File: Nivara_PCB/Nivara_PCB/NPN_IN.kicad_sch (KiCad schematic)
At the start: 5 parts, among them U6 LTV-357T

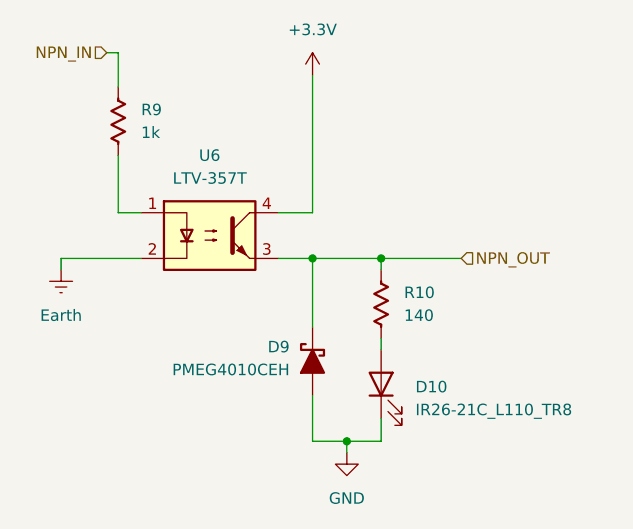
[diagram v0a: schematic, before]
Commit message: Cambios finales en la comprobación del DRC.
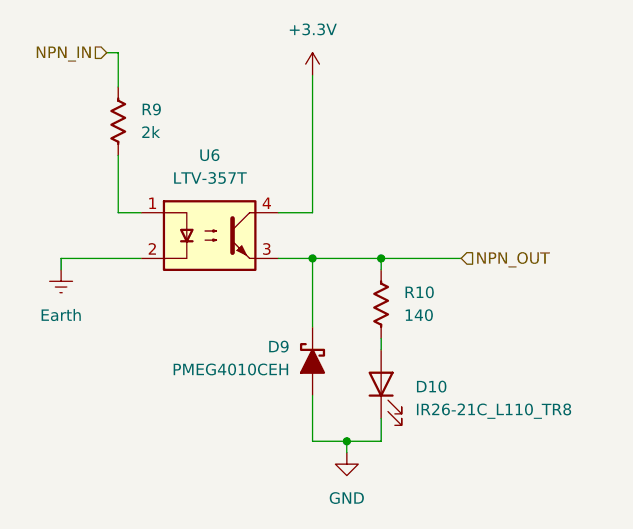
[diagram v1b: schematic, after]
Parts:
- R9: value 1k -> 2k
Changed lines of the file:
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@@
 			)
 		)
-		(property "Value" "1k"
+		(property "Value" "2k"
 			(at 107.95 68.5799 0)
 			(effects

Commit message: TERMINACIONES Y AJUSTES FINALES
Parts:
- removed D10: IR26-21C_L110_TR8, LED_SMD:LED_1206_3216Metric, symbol LED:IR26-21C_L110_TR8
- added D11: LED, LED_SMD:LED_0603_1608Metric, symbol EasyEDA:LED
- D10: renamed from D9; LCSC Part (none) -> C193342; Part # (none) -> PMEG4010CEH,115
- R13: renamed from R9; LCSC Part (none) -> C22975; Part # (none) -> 0603WAF2001T5E
- R14: renamed from R10; LCSC Part (none) -> C245910; Part # (none) -> RC0603FR-07140RL
- U8: renamed from U6; LCSC Part (none) -> C119091; Part # (none) -> LTV-357T-C
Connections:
- net GND: now also D11.1 (K)
- net at R14.2: now also D11.2 (A)
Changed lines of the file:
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@@
 		(dnp no)
 		(fields_autoplaced yes)
-		(property "Reference" "#PWR027"
+		(property "Reference" "#PWR031"
 			(at 127 66.04 0)
 			(effects
@@
 			(project "Nivara_PCB"
 				(path "/13184db0-a71d-4054-b13a-bbf46d2b100d/4e7fa7f2-8bf5-4f9c-874d-fa1b4fd76f92/0a310172-7d8e-4fb6-834e-e52959d34ba2"
-					(reference "#PWR055")
-					(unit 1)
-				)
-				(path "/13184db0-a71d-4054-b13a-bbf46d2b100d/4e7fa7f2-8bf5-4f9c-874d-fa1b4fd76f92/58467d6c-1433-4318-a1ea-3b041dc0b319"
-					(reference "#PWR027")
+					(reference "#PWR059")
+					(unit 1)
+				)
+				(path "/13184db0-a71d-4054-b13a-bbf46d2b100d/4e7fa7f2-8bf5-4f9c-874d-fa1b4fd76f92/58467d6c-1433-4318-a1ea-3b041dc0b319"
+					(reference "#PWR031")
 					(unit 1)
 				)
@@
 		(dnp no)
 		(fields_autoplaced yes)
-		(property "Reference" "#PWR028"
+		(property "Reference" "#PWR032"
 			(at 130.81 110.49 0)
 			(effects
@@
 			(project "Nivara_PCB"
 				(path "/13184db0-a71d-4054-b13a-bbf46d2b100d/4e7fa7f2-8bf5-4f9c-874d-fa1b4fd76f92/0a310172-7d8e-4fb6-834e-e52959d34ba2"
-					(reference "#PWR056")
-					(unit 1)
-				)
-				(path "/13184db0-a71d-4054-b13a-bbf46d2b100d/4e7fa7f2-8bf5-4f9c-874d-fa1b4fd76f92/58467d6c-1433-4318-a1ea-3b041dc0b319"
-					(reference "#PWR028")
+					(reference "#PWR060")
+					(unit 1)
+				)
+				(path "/13184db0-a71d-4054-b13a-bbf46d2b100d/4e7fa7f2-8bf5-4f9c-874d-fa1b4fd76f92/58467d6c-1433-4318-a1ea-3b041dc0b319"
+					(reference "#PWR032")
 					(unit 1)
 				)
@@
 		(on_board yes)
 		(dnp no)
-		(property "Reference" "D9"
+		(property "Reference" "D10"
 			(at 124.46 92.3924 90)
 			(effects
@@
 			)
 		)
-		(property "Datasheet" "https://www.tme.eu/Document/6076ddfe18935c4c311aad91dddcf920/PMEG4010CEX-DTE.pdf"
+		(property "Datasheet" "https://www.lcsc.com/datasheet/C193342.pdf"
 			(at 127 93.98 0)
 			(effects
@@
 			)
 		)
+		(property "Part #" "PMEG4010CEH,115"
+			(at 127 93.98 90)
+			(effects
+				(font
+					(size 1.27 1.27)
+				)
+				(hide yes)
+			)
+		)
+		(property "LCSC Part" "C193342"
+			(at 127 93.98 90)
+			(effects
+				(font
+					(size 1.27 1.27)
+				)
+				(hide yes)
+			)
+		)
 		(pin "1"
 		)
@@
 			(project "Nivara_PCB"
 				(path "/13184db0-a71d-4054-b13a-bbf46d2b100d/4e7fa7f2-8bf5-4f9c-874d-fa1b4fd76f92/0a310172-7d8e-4fb6-834e-e52959d34ba2"
-					(reference "D24")
-					(unit 1)
-				)
-				(path "/13184db0-a71d-4054-b13a-bbf46d2b100d/4e7fa7f2-8bf5-4f9c-874d-fa1b4fd76f92/58467d6c-1433-4318-a1ea-3b041dc0b319"
-					(reference "D9")
+					(reference "D25")
+					(unit 1)
+				)
+				(path "/13184db0-a71d-4054-b13a-bbf46d2b100d/4e7fa7f2-8bf5-4f9c-874d-fa1b4fd76f92/58467d6c-1433-4318-a1ea-3b041dc0b319"
+					(reference "D10")
 					(unit 1)
 				)
@@
 		(dnp no)
 		(fields_autoplaced yes)
-		(property "Reference" "#PWR083"
+		(property "Reference" "#PWR030"
 			(at 99.06 90.17 0)
 			(effects
@@
 			(project ""
 				(path "/13184db0-a71d-4054-b13a-bbf46d2b100d/4e7fa7f2-8bf5-4f9c-874d-fa1b4fd76f92/0a310172-7d8e-4fb6-834e-e52959d34ba2"
-					(reference "#PWR084")
-					(unit 1)
-				)
-				(path "/13184db0-a71d-4054-b13a-bbf46d2b100d/4e7fa7f2-8bf5-4f9c-874d-fa1b4fd76f92/58467d6c-1433-4318-a1ea-3b041dc0b319"
-					(reference "#PWR083")
+					(reference "#PWR058")
+					(unit 1)
+				)
+				(path "/13184db0-a71d-4054-b13a-bbf46d2b100d/4e7fa7f2-8bf5-4f9c-874d-fa1b4fd76f92/58467d6c-1433-4318-a1ea-3b041dc0b319"
+					(reference "#PWR030")
 					(unit 1)
 				)
@@
 	)
 	(symbol
-		(lib_id "LED:IR26-21C_L110_TR8")
-		(at 134.62 96.52 90)
+		(lib_id "EasyEDA:LED")
+		(at 134.62 96.52 270)
+		(mirror x)
 		(unit 1)
 		(exclude_from_sim no)
@@
 		(on_board yes)
 		(dnp no)
-		(fields_autoplaced yes)
-		(property "Reference" "D10"
-			(at 138.43 96.8374 90)
+		(property "Reference" "D11"
+			(at 144.272 96.52 90)
 			(effects
 				(font
@@
 			)
 		)
-		(property "Value" "IR26-21C_L110_TR8"
-			(at 138.43 99.3774 90)
+		(property "Value" "LED"
+			(at 144.272 99.06 90)
 			(effects
 				(font
@@
 			)
 		)
-		(property "Footprint" "LED_SMD:LED_1206_3216Metric"
-			(at 129.54 96.52 0)
-			(effects
-				(font
-					(size 1.27 1.27)
-				)
-				(hide yes)
-			)
-		)
-		(property "Datasheet" "http://www.everlight.com/file/ProductFile/IR26-21C-L110-TR8.pdf"
+		(property "Footprint" "LED_SMD:LED_0603_1608Metric"
 			(at 134.62 96.52 0)
 			(effects
@@
 			)
 		)
-		(property "Description" "940nm, 20 deg, Infrared LED, 1206"
+		(property "Datasheet" "https://www.lcsc.com/datasheet/C440520.pdf"
 			(at 134.62 96.52 0)
 			(effects
@@
 			)
 		)
+		(property "Description" "Light emitting diode"
+			(at 134.62 96.52 0)
+			(effects
+				(font
+					(size 1.27 1.27)
+				)
+				(hide yes)
+			)
+		)
+		(property "Sim.Pins" "1=K 2=A"
+			(at 134.62 96.52 0)
+			(effects
+				(font
+					(size 1.27 1.27)
+				)
+				(hide yes)
+			)
+		)
+		(property "LCSC Part" "C12065"
+			(at 134.62 96.52 90)
+			(effects
+				(font
+					(size 1.27 1.27)
+				)
+				(hide yes)
+			)
+		)
+		(property "Part #" "LTST-C193TGKT-5A"
+			(at 134.62 96.52 90)
+			(effects
+				(font
+					(size 1.27 1.27)
+				)
+				(hide yes)
+			)
+		)
+		(pin "1"
+		)
 		(pin "2"
 		)
-		(pin "1"
-		)
 		(instances
 			(project "Nivara_PCB"
 				(path "/13184db0-a71d-4054-b13a-bbf46d2b100d/4e7fa7f2-8bf5-4f9c-874d-fa1b4fd76f92/0a310172-7d8e-4fb6-834e-e52959d34ba2"
+					(reference "D26")
+					(unit 1)
+				)
+				(path "/13184db0-a71d-4054-b13a-bbf46d2b100d/4e7fa7f2-8bf5-4f9c-874d-fa1b4fd76f92/58467d6c-1433-4318-a1ea-3b041dc0b319"
 					(reference "D11")
-					(unit 1)
-				)
-				(path "/13184db0-a71d-4054-b13a-bbf46d2b100d/4e7fa7f2-8bf5-4f9c-874d-fa1b4fd76f92/58467d6c-1433-4318-a1ea-3b041dc0b319"
-					(reference "D10")
 					(unit 1)
 				)
@@
 		(dnp no)
 		(fields_autoplaced yes)
-		(property "Reference" "R9"
+		(property "Reference" "R13"
 			(at 107.95 66.0399 0)
 			(effects
@@
 			)
 		)
-		(property "Datasheet" "~"
+		(property "Datasheet" "https://jlcpcb.com/api/file/downloadByFileSystemAccessId/8579706189568917504"
 			(at 105.41 67.31 0)
 			(effects
@@
 			)
 		)
+		(property "Part #" "0603WAF2001T5E"
+			(at 105.41 67.31 0)
+			(effects
+				(font
+					(size 1.27 1.27)
+				)
+				(hide yes)
+			)
+		)
+		(property "LCSC Part" "C22975"
+			(at 105.41 67.31 0)
+			(effects
+				(font
+					(size 1.27 1.27)
+				)
+				(hide yes)
+			)
+		)
 		(pin "2"
 		)
@@
 			(project "Nivara_PCB"
 				(path "/13184db0-a71d-4054-b13a-bbf46d2b100d/4e7fa7f2-8bf5-4f9c-874d-fa1b4fd76f92/0a310172-7d8e-4fb6-834e-e52959d34ba2"
-					(reference "R33")
-					(unit 1)
-				)
-				(path "/13184db0-a71d-4054-b13a-bbf46d2b100d/4e7fa7f2-8bf5-4f9c-874d-fa1b4fd76f92/58467d6c-1433-4318-a1ea-3b041dc0b319"
-					(reference "R9")
+					(reference "R39")
+					(unit 1)
+				)
+				(path "/13184db0-a71d-4054-b13a-bbf46d2b100d/4e7fa7f2-8bf5-4f9c-874d-fa1b4fd76f92/58467d6c-1433-4318-a1ea-3b041dc0b319"
+					(reference "R13")
 					(unit 1)
 				)
@@
 		(dnp no)
 		(fields_autoplaced yes)
-		(property "Reference" "U6"
+		(property "Reference" "U8"
 			(at 115.57 71.12 0)
 			(effects
@@
 			)
 		)
-		(property "Datasheet" "https://www.buerklin.com/medias/sys_master/download/download/h91/ha0/8892020588574.pdf"
+		(property "Datasheet" "https://www.lcsc.com/datasheet/C119091.pdf"
 			(at 115.57 80.01 0)
 			(effects
@@
 			)
 		)
+		(property "Part #" "LTV-357T-C"
+			(at 115.57 80.01 0)
+			(effects
+				(font
+					(size 1.27 1.27)
+				)
+				(hide yes)
+			)
+		)
+		(property "LCSC Part" "C119091"
+			(at 115.57 80.01 0)
+			(effects
+				(font
+					(size 1.27 1.27)
+				)
+				(hide yes)
+			)
+		)
 		(pin "3"
 		)
@@
 			(project "Nivara_PCB"
 				(path "/13184db0-a71d-4054-b13a-bbf46d2b100d/4e7fa7f2-8bf5-4f9c-874d-fa1b4fd76f92/0a310172-7d8e-4fb6-834e-e52959d34ba2"
-					(reference "U14")
-					(unit 1)
-				)
-				(path "/13184db0-a71d-4054-b13a-bbf46d2b100d/4e7fa7f2-8bf5-4f9c-874d-fa1b4fd76f92/58467d6c-1433-4318-a1ea-3b041dc0b319"
-					(reference "U6")
+					(reference "U16")
+					(unit 1)
+				)
+				(path "/13184db0-a71d-4054-b13a-bbf46d2b100d/4e7fa7f2-8bf5-4f9c-874d-fa1b4fd76f92/58467d6c-1433-4318-a1ea-3b041dc0b319"
+					(reference "U8")
 					(unit 1)
 				)
@@
 		(dnp no)
 		(fields_autoplaced yes)
-		(property "Reference" "R10"
+		(property "Reference" "R14"
 			(at 137.16 86.3599 0)
 			(effects
@@
 			)
 		)
-		(property "Datasheet" "~"
+		(property "Datasheet" "https://www.lcsc.com/datasheet/C245910.pdf"
 			(at 134.62 87.63 0)
 			(effects
@@
 			)
 		)
+		(property "Part #" "RC0603FR-07140RL"
+			(at 134.62 87.63 0)
+			(effects
+				(font
+					(size 1.27 1.27)
+				)
+				(hide yes)
+			)
+		)
+		(property "LCSC Part" "C245910"
+			(at 134.62 87.63 0)
+			(effects
+				(font
+					(size 1.27 1.27)
+				)
+				(hide yes)
+			)
+		)
 		(pin "2"
 		)
@@
 			(project "Nivara_PCB"
 				(path "/13184db0-a71d-4054-b13a-bbf46d2b100d/4e7fa7f2-8bf5-4f9c-874d-fa1b4fd76f92/0a310172-7d8e-4fb6-834e-e52959d34ba2"
-					(reference "R34")
-					(unit 1)
-				)
-				(path "/13184db0-a71d-4054-b13a-bbf46d2b100d/4e7fa7f2-8bf5-4f9c-874d-fa1b4fd76f92/58467d6c-1433-4318-a1ea-3b041dc0b319"
-					(reference "R10")
-					(unit 1)
-				)
+					(reference "R40")
+					(unit 1)
+				)
+				(path "/13184db0-a71d-4054-b13a-bbf46d2b100d/4e7fa7f2-8bf5-4f9c-874d-fa1b4fd76f92/58467d6c-1433-4318-a1ea-3b041dc0b319"
+					(reference "R14")
+					(unit 1)
+				)
